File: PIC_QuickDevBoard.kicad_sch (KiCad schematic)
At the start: 33 parts, among them J1 PICKitConnector, J10 Conn_01x08_Pin, J2 PowerSource, J3 USB_B_Micro, J4 Conn_01x08_Pin, J9 Conn_01x08_Pin, SW1 SW_Push, U1 PIC24, U2 PIC16, U3 LD1117, Y1 Crystal

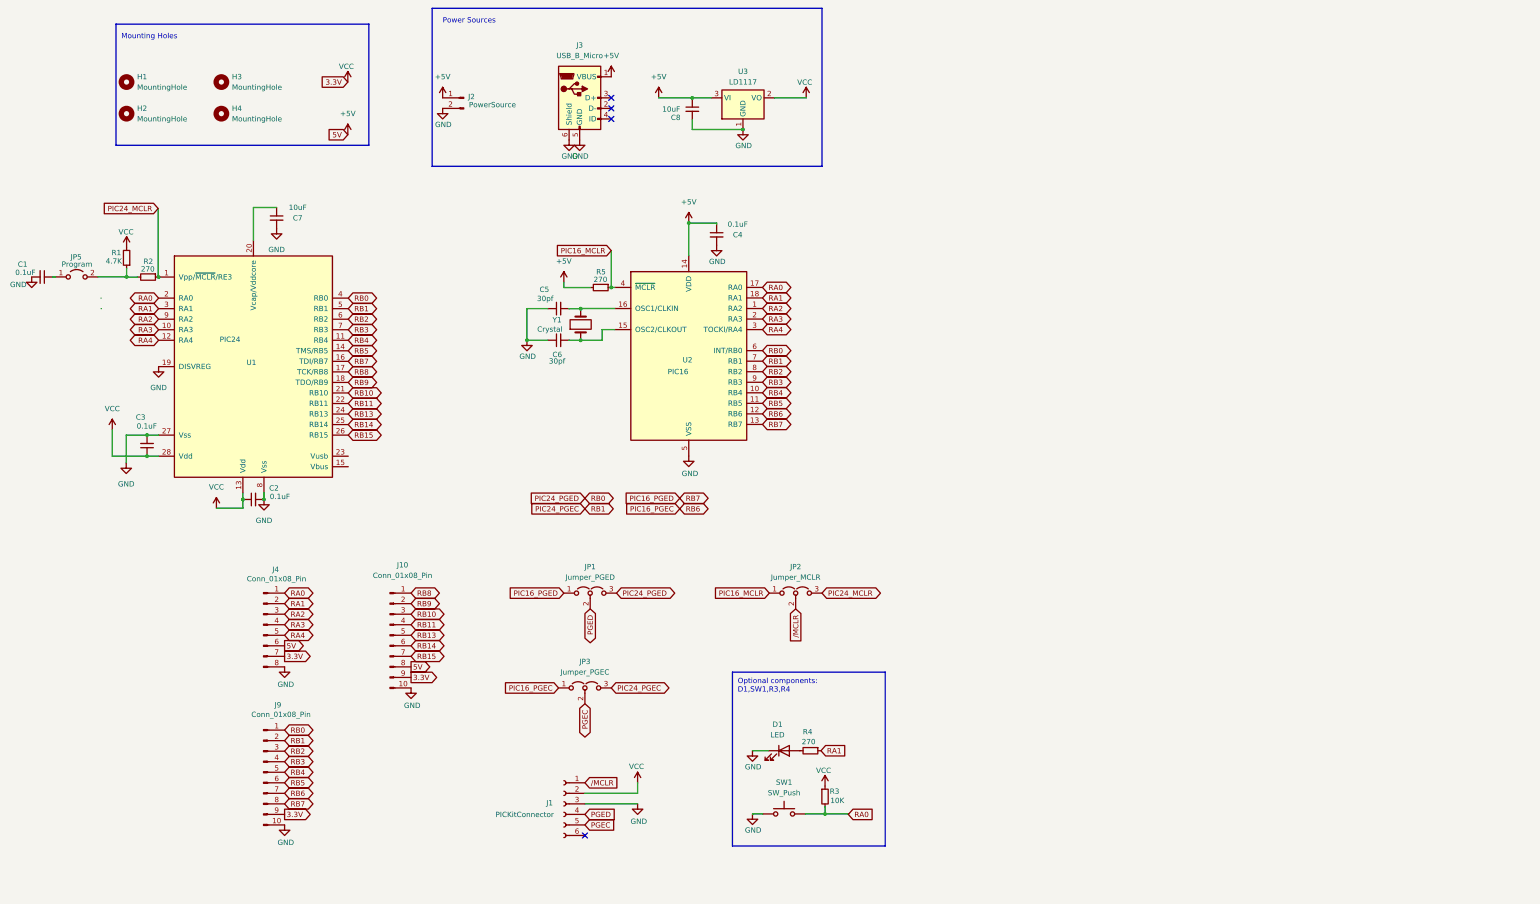
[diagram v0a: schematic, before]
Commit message: fixing PICF14 vcc
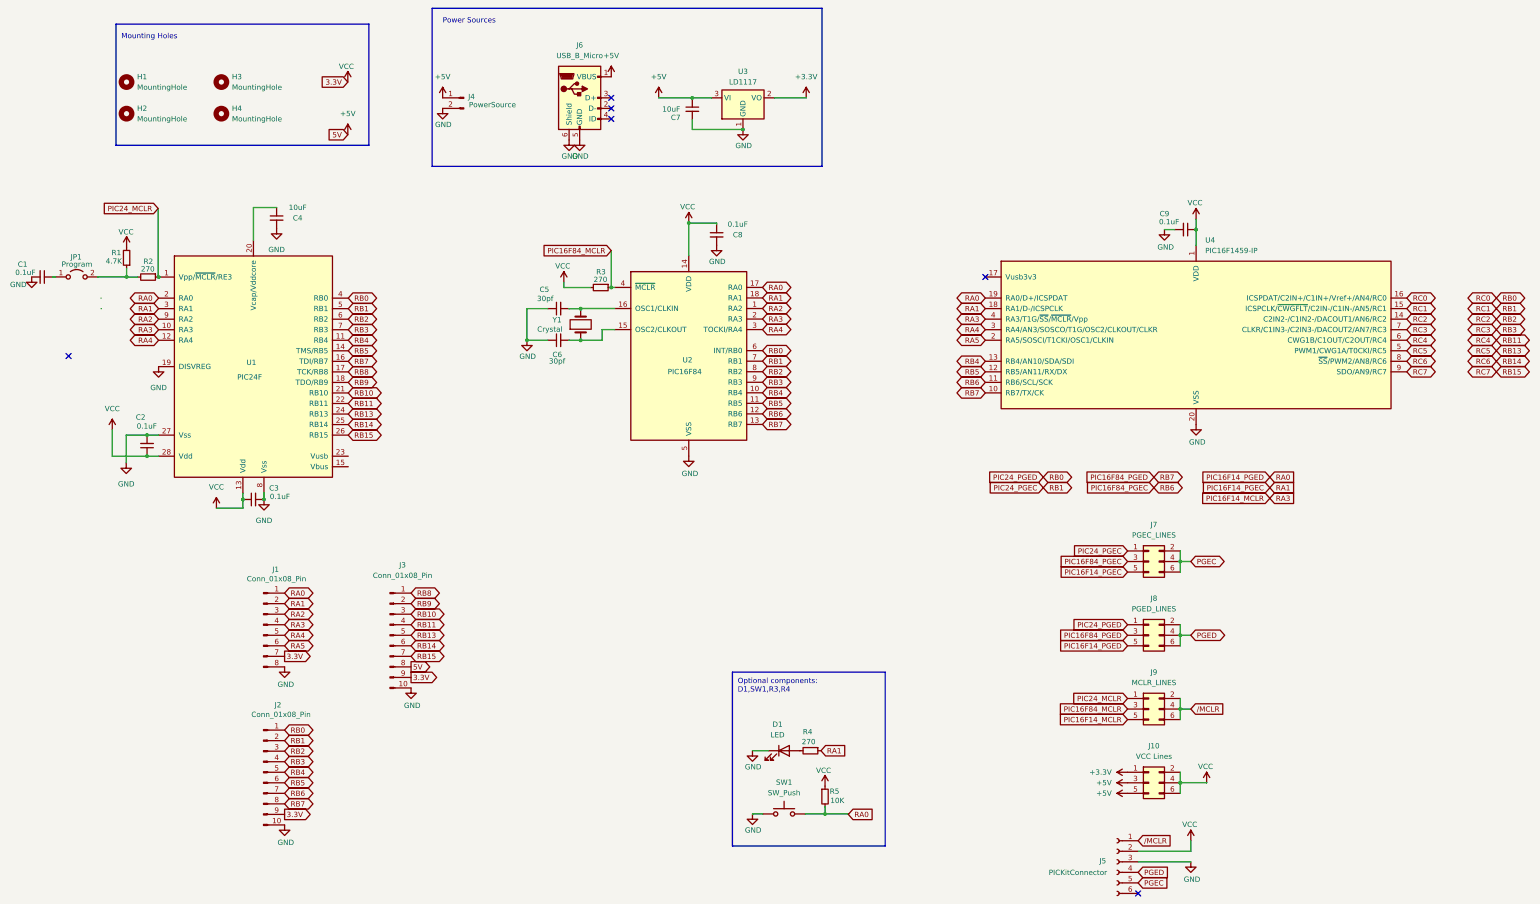
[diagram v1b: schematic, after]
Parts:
- removed JP1: Jumper_PGED, Connector_PinHeader_2.54mm:PinHeader_1x03_P2.54mm_Vertical, symbol Jumper:Jumper_3_Open
- removed JP2: Jumper_MCLR, Connector_PinHeader_2.54mm:PinHeader_1x03_P2.54mm_Vertical, symbol Jumper:Jumper_3_Open
- removed JP3: Jumper_PGEC, Connector_PinHeader_2.54mm:PinHeader_1x03_P2.54mm_Vertical, symbol Jumper:Jumper_3_Open
- added C9: 0.1uF, Capacitor_THT:C_Disc_D3.4mm_W2.1mm_P2.50mm, symbol Device:C_Small
- added J10: VCC Lines, Connector_PinHeader_2.00mm:PinHeader_2x03_P2.00mm_Vertical, symbol Connector_Generic:Conn_02x03_Odd_Even
- added J7: PGEC_LINES, Connector_PinHeader_2.00mm:PinHeader_2x03_P2.00mm_Vertical, symbol Connector_Generic:Conn_02x03_Odd_Even
- added J8: PGED_LINES, Connector_PinHeader_2.00mm:PinHeader_2x03_P2.00mm_Vertical, symbol Connector_Generic:Conn_02x03_Odd_Even
- added J9: MCLR_LINES, Connector_PinHeader_2.00mm:PinHeader_2x03_P2.00mm_Vertical, symbol Connector_Generic:Conn_02x03_Odd_Even
- added U4: PIC16F1459-IP, Package_DIP:DIP-20_W7.62mm, symbol MCU_Microchip_PIC16:PIC16F1459-IP
- J6: renamed from J3; footprint Roni Footprints:USB_Mini-B_Tensility_4Holes -> Roni_Footprints:USB_Mini-B_Tensility_4Holes
- SW1: footprint Button_Switch_THT:SW_PUSH_6mm -> Roni_Footprints:SW_PUSH_6mm_2Holes
- U1: value PIC24 -> PIC24F
- U2: value PIC16 -> PIC16F84
- renumbered C3 to C2, C2 to C3, C7 to C4, C8 to C7, C4 to C8, J4 to J1, J9 to J2, J10 to J3, J2 to J4, J1 to J5, JP5 to JP1, R5 to R3, R3 to R5
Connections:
- net +5V: now also J10.3 (Pin_3), J10.5 (Pin_5); no longer C8.1, J1.6 (Pin_6), R3.2, U2.14 (VDD)
- net GND: now also C9.2, U4.20 (VSS)
- net PGEC: now also J7.2 (Pin_2), J7.4 (Pin_4), J7.6 (Pin_6)
- net PGED: now also J8.2 (Pin_2), J8.4 (Pin_4), J8.6 (Pin_6)
- net PIC24_MCLR: now also J9.1 (Pin_1)
- net PIC24_PGEC: now also J7.1 (Pin_1), U4.15 (ICSPCLK/~{CWGFLT}/C2IN-/C1IN-/AN5/RC1)
- net PIC24_PGED: now also J8.1 (Pin_1), U4.16 (ICSPDAT/C2IN+/C1IN+/Vref+/AN4/RC0)
- net RA4: now also U4.3 (RA4/AN3/SOSCO/T1G/OSC2/CLKOUT/CLKR)
- net RB11: now also U4.6 (CWG1B/C1OUT/C2OUT/RC4)
- net RB13: now also U4.5 (PWM1/CWG1A/T0CKI/RC5)
- net RB14: now also U4.8 (~{SS}/PWM2/AN8/RC6)
- net RB15: now also U4.9 (SDO/AN9/RC7)
- net RB2: now also U4.14 (C2IN2-/C1IN2-/DACOUT1/AN6/RC2)
- net RB3: now also U4.7 (CLKR/C1IN3-/C2IN3-/DACOUT2/AN7/RC3)
- net RB4: now also U4.13 (RB4/AN10/SDA/SDI)
- net RB5: now also U4.12 (RB5/AN11/RX/DX)
- net VCC: now also C8.1, R3.2, U2.14 (VDD), C9.1, J10.2 (Pin_2), J10.4 (Pin_4), J10.6 (Pin_6), U4.1 (VDD); no longer U3.2 (VO)
- net /MCLR: now also J9.2 (Pin_2), J9.4 (Pin_4), J9.6 (Pin_6)
- net PIC16_MCLR renamed PIC16F84_MCLR
- net PIC16F84_MCLR: now also J9.3 (Pin_3)
- net PIC16_PGEC renamed PIC16F84_PGEC
- net PIC16F84_PGEC: now also J7.3 (Pin_3), U4.11 (RB6/SCL/SCK)
- net PIC16_PGED renamed PIC16F84_PGED
- net PIC16F84_PGED: now also J8.3 (Pin_3), U4.10 (RB7/TX/CK)
- net RA0 renamed PIC16F14_PGED
- net PIC16F14_PGED: now also J8.5 (Pin_5), U4.19 (RA0/D+/ICSPDAT)
- net RA1 renamed PIC16F14_PGEC
- net PIC16F14_PGEC: now also J7.5 (Pin_5), U4.18 (RA1/D-/ICSPCLK)
- net RA3 renamed PIC16F14_MCLR
- net PIC16F14_MCLR: now also J9.5 (Pin_5), U4.4 (RA3/T1G/~{SS}/~{MCLR}/Vpp)
- new net +3.3V: J10.1 (Pin_1), U3.2 (VO)
- new net RA5: J1.6 (Pin_6), U4.2 (RA5/SOSCI/T1CKI/OSC1/CLKIN)
- no-connect marks 4 -> 6
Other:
- moved on the sheet: J5

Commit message: Updated PCB to REv 2.1 with fix to VCC for PIC16F
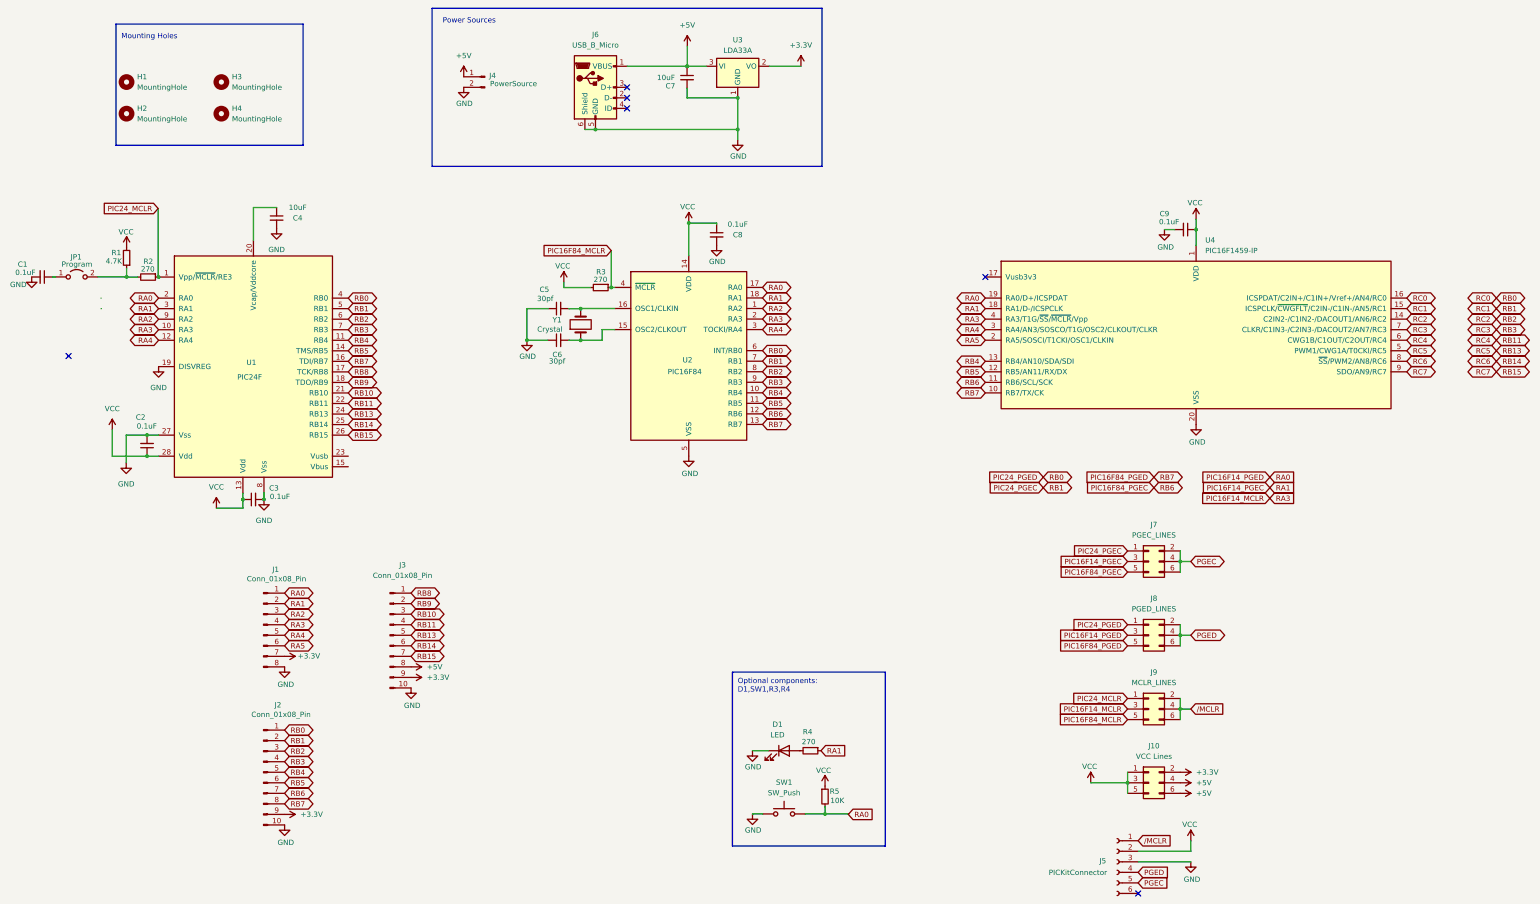
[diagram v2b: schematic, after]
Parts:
- U3: value LD1117 -> LDA33A
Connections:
- net +3.3V: now also J1.7 (Pin_7), J10.2 (Pin_2), J2.9 (Pin_9), J3.9 (Pin_9); no longer J10.1 (Pin_1)
- net +5V: now also J10.4 (Pin_4), J10.6 (Pin_6); no longer J10.3 (Pin_3), J10.5 (Pin_5)
- net PIC16F14_MCLR: now also J9.3 (Pin_3); no longer J9.5 (Pin_5)
- net PIC16F14_PGEC: now also J7.3 (Pin_3); no longer J7.5 (Pin_5)
- net PIC16F14_PGED: now also J8.3 (Pin_3); no longer J8.5 (Pin_5)
- net PIC16F84_MCLR: now also J9.5 (Pin_5); no longer J9.3 (Pin_3)
- net PIC16F84_PGEC: now also J7.5 (Pin_5); no longer J7.3 (Pin_3)
- net PIC16F84_PGED: now also J8.5 (Pin_5); no longer J8.3 (Pin_3)
- net VCC: now also J10.1 (Pin_1), J10.3 (Pin_3), J10.5 (Pin_5); no longer J1.7 (Pin_7), J10.2 (Pin_2), J10.4 (Pin_4), J10.6 (Pin_6), J2.9 (Pin_9), J3.9 (Pin_9)
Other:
- moved on the sheet: C7, J4, J6, U3

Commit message: Revision 2.2
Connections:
- net PIC24_PGEC is gone; now on net PIC16F14_PGEC: J2.2 (Pin_2), J7.1 (Pin_1), U1.5 (RB1), U2.7 (RB1), U4.15 (ICSPCLK/~{CWGFLT}/C2IN-/C1IN-/AN5/RC1)
- net PIC24_PGED is gone; now on net PIC16F14_PGED: J2.1 (Pin_1), J8.1 (Pin_1), U1.4 (RB0), U2.6 (INT/RB0), U4.16 (ICSPDAT/C2IN+/C1IN+/Vref+/AN4/RC0)
- net PIC16F14_PGEC: no longer J1.2 (Pin_2), R4.1, U1.3 (RA1), U2.18 (RA1), U4.18 (RA1/D-/ICSPCLK)
- net PIC16F14_PGED: no longer J1.1 (Pin_1), R5.2, SW1.2, U1.2 (RA0), U2.17 (RA0), U4.19 (RA0/D+/ICSPDAT)
- new net RA0: J1.1 (Pin_1), R5.2, SW1.2, U1.2 (RA0), U2.17 (RA0), U4.19 (RA0/D+/ICSPDAT)
- new net RA1: J1.2 (Pin_2), R4.1, U1.3 (RA1), U2.18 (RA1), U4.18 (RA1/D-/ICSPCLK)
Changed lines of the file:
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@@
 	(title_block
 		(title "PIC24 & PIC16F84 Programmer & Dev Board")
-		(date "2024-04-13")
-		(rev "2.1")
+		(date "2024-05-01")
+		(rev "2.2")
 		(company "RCC 2024")
 		(comment 1 "https://github.com/costarc/PIC_QuickDevBoard")
@@
 		)
 	)
+	(global_label "RC0"
+		(shape input)
+		(at 341.63 146.05 0)
+		(fields_autoplaced yes)
+		(effects
+			(font
+				(size 1.27 1.27)
+			)
+			(justify left)
+		)
+		(property "Intersheetrefs" "${INTERSHEET_REFS}"
+			(at 348.3647 146.05 0)
+			(effects
+				(font
+					(size 1.27 1.27)
+				)
+				(justify left)
+				(hide yes)
+			)
+		)
+	)
 	(global_label "RB5"
 		(shape bidirectional)
@@
 		)
 	)
+	(global_label "RC1"
+		(shape input)
+		(at 341.63 148.59 0)
+		(fields_autoplaced yes)
+		(effects
+			(font
+				(size 1.27 1.27)
+			)
+			(justify left)
+		)
+		(property "Intersheetrefs" "${INTERSHEET_REFS}"
+			(at 348.3647 148.59 0)
+			(effects
+				(font
+					(size 1.27 1.27)
+				)
+				(justify left)
+				(hide yes)
+			)
+		)
+	)
 	(global_label "PIC16F84_MCLR"
 		(shape input)
@@
 		)
 	)
-	(global_label "RA0"
-		(shape input)
-		(at 341.63 146.05 0)
-		(fields_autoplaced yes)
-		(effects
-			(font
-				(size 1.27 1.27)
-			)
-			(justify left)
-		)
-		(property "Intersheetrefs" "${INTERSHEET_REFS}"
-			(at 348.1833 146.05 0)
-			(effects
-				(font
-					(size 1.27 1.27)
-				)
-				(justify left)
-				(hide yes)
-			)
-		)
-	)
 	(global_label "RC0"
 		(shape bidirectional)
@@
 			(effects
 				(font
-					(size 1.27 1.27)
-				)
-				(justify left)
-				(hide yes)
-			)
-		)
-	)
-	(global_label "RA1"
-		(shape input)
-		(at 341.63 148.59 0)
-		(fields_autoplaced yes)
-		(effects
-			(font
-				(size 1.27 1.27)
-			)
-			(justify left)
-		)
-		(property "Intersheetrefs" "${INTERSHEET_REFS}"
-			(at 348.1833 148.59 0)
-			(effects
-				(font

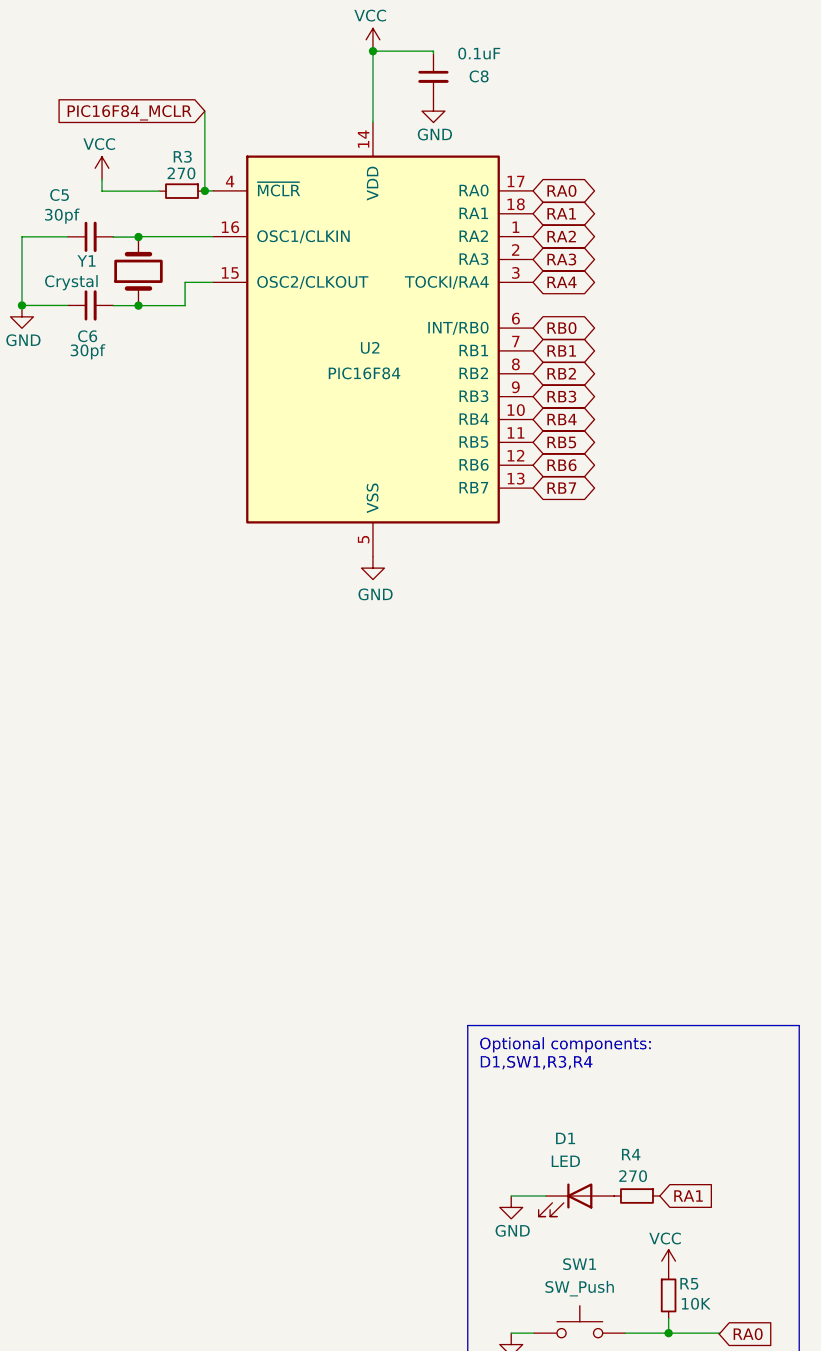
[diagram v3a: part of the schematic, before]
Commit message: Rev2.3 - fixed mini-usb footprint and pcb routing power from it.
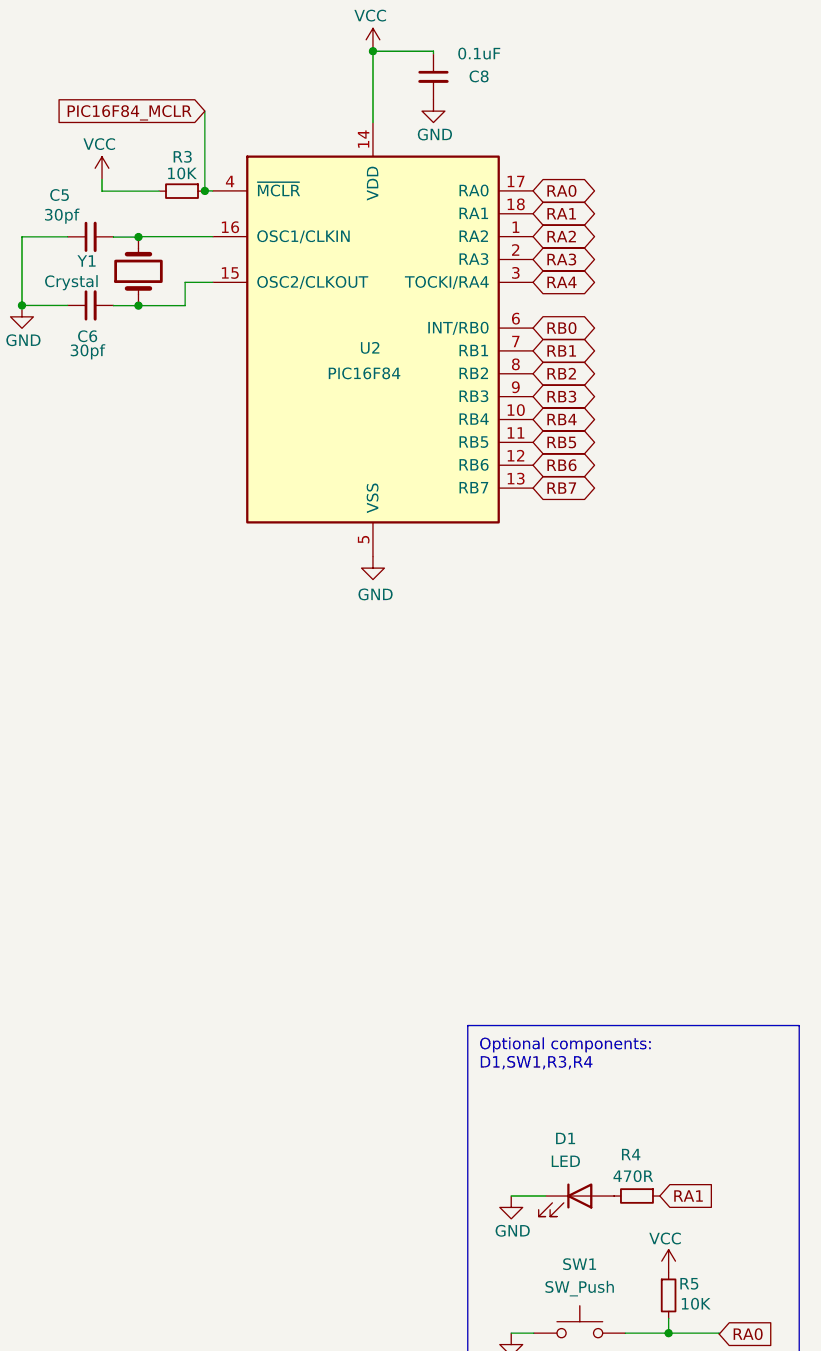
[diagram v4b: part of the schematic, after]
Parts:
- R3: value 270 -> 10K
- R4: value 270 -> 470R
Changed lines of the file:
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@@
 	(title_block
 		(title "PIC24 & PIC16F84 Programmer & Dev Board")
-		(date "2024-05-01")
-		(rev "2.2")
+		(date "2024-05-17")
+		(rev "2.3")
 		(company "RCC 2024")
 		(comment 1 "https://github.com/costarc/PIC_QuickDevBoard")
@@
 			)
 		)
-		(property "Value" "270"
+		(property "Value" "10K"
 			(at 180.2756 98.4066 90)
 			(effects
@@
 			)
 		)
-		(property "Value" "270"
+		(property "Value" "470R"
 			(at 230.4591 209.823 90)
 			(effects
